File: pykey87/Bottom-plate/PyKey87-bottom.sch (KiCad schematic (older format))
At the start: 9 parts

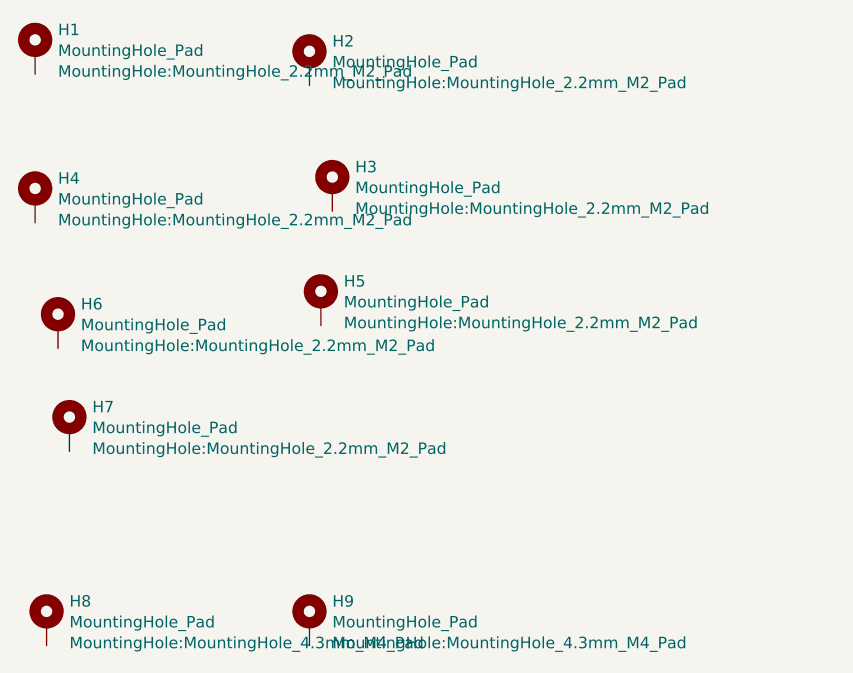
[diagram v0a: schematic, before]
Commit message: Moving things around
Prep for merging. Also did some clean up and added 8th standoff.
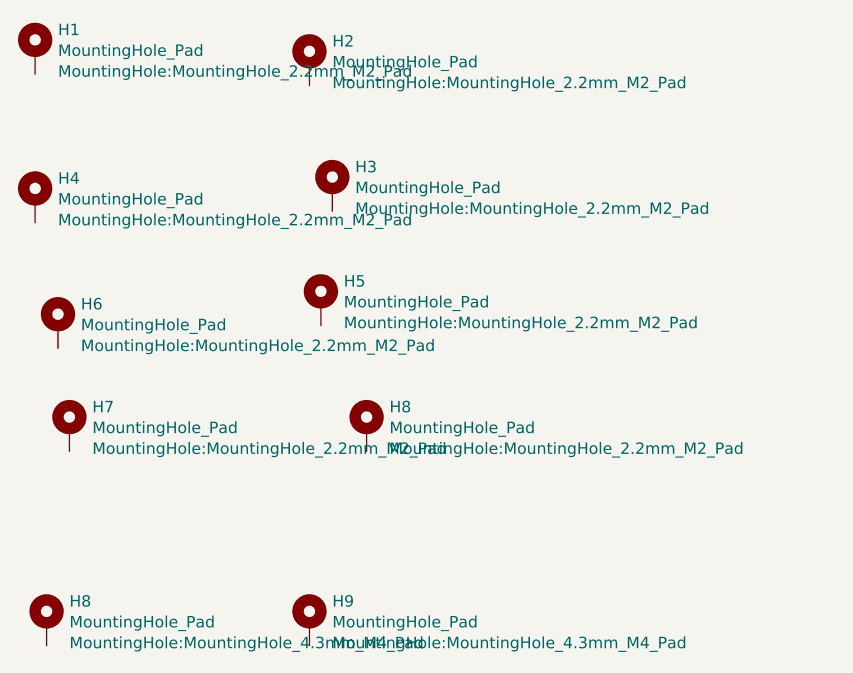
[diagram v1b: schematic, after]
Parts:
- added H8: MountingHole_Pad, MountingHole:MountingHole_2.2mm_M2_Pad, symbol Mechanical:MountingHole_Pad
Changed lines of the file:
@@
+	1    0    0    -1
+$EndComp
+$Comp
+L Mechanical:MountingHole_Pad H8
+U 1 1 618F6366
+P 3750 4150
+F 0 "H8" H 3850 4244 50  0000 L CNN
+F 1 "MountingHole_Pad" H 3850 4153 50  0000 L CNN
+F 2 "MountingHole:MountingHole_2.2mm_M2_Pad" H 3850 4062 50  0000 L CNN
+F 3 "~" H 3750 4150 50  0001 C CNN
+	1    3750 4150
 	1    0    0    -1
 $EndComp

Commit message: Working on issues
https://github.com/jpconstantineau/PyKey60/issues/3
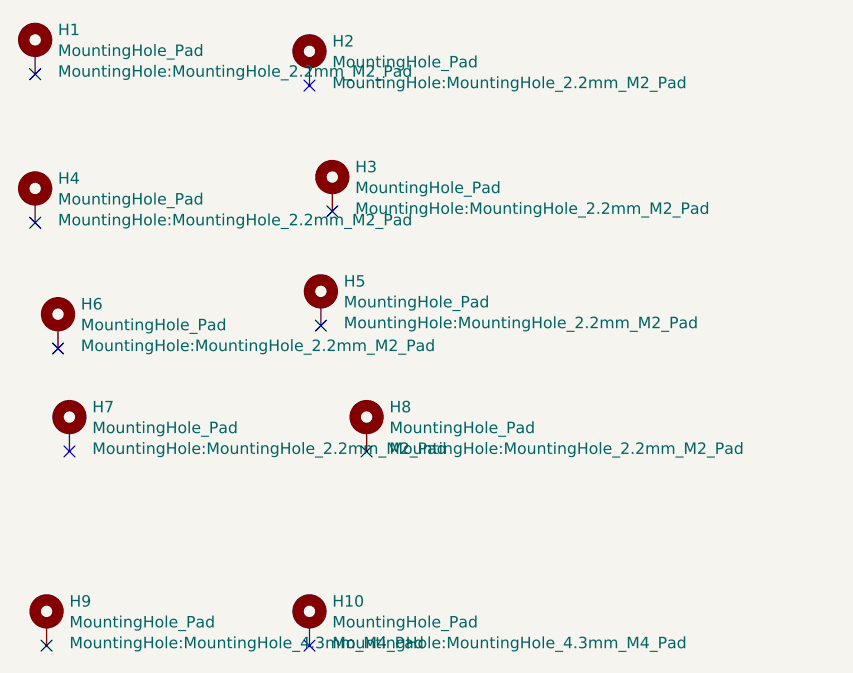
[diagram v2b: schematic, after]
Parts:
- renumbered H9 to H10, H8 to H9
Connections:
- no-connect marks 0 -> 10
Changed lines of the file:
@@
-$EndComp
-$Comp
-L Mechanical:MountingHole_Pad H1
-U 1 1 618E2AF4
-P 2300 2500
-F 0 "H1" H 2400 2594 50  0000 L CNN
-F 1 "MountingHole_Pad" H 2400 2503 50  0000 L CNN
-F 2 "MountingHole:MountingHole_2.2mm_M2_Pad" H 2400 2412 50  0000 L CNN
-F 3 "~" H 2300 2500 50  0001 C CNN
-	1    2300 2500
-	1    0    0    -1
 $EndComp
 $Comp
@@
 $EndComp
 $Comp
-L Mechanical:MountingHole_Pad H8
+L Mechanical:MountingHole_Pad H9
 U 1 1 618E47BC
 P 2350 5000
-F 0 "H8" H 2450 5094 50  0000 L CNN
+F 0 "H9" H 2450 5094 50  0000 L CNN
 F 1 "MountingHole_Pad" H 2450 5003 50  0000 L CNN
 F 2 "MountingHole:MountingHole_4.3mm_M4_Pad" H 2450 4912 50  0000 L CNN
@@
 $EndComp
 $Comp
-L Mechanical:MountingHole_Pad H9
+L Mechanical:MountingHole_Pad H10
 U 1 1 618E4FDD
 P 3500 5000
-F 0 "H9" H 3600 5094 50  0000 L CNN
+F 0 "H10" H 3600 5094 50  0000 L CNN
 F 1 "MountingHole_Pad" H 3600 5003 50  0000 L CNN
 F 2 "MountingHole:MountingHole_4.3mm_M4_Pad" H 3600 4912 50  0000 L CNN
@@
 	1    0    0    -1
 $EndComp
+$Comp
+L Mechanical:MountingHole_Pad H1
+U 1 1 618E2AF4
+P 2300 2500
+F 0 "H1" H 2400 2594 50  0000 L CNN
+F 1 "MountingHole_Pad" H 2400 2503 50  0000 L CNN
+F 2 "MountingHole:MountingHole_2.2mm_M2_Pad" H 2400 2412 50  0000 L CNN
+F 3 "~" H 2300 2500 50  0001 C CNN
+	1    2300 2500
+	1    0    0    -1
+$EndComp
+NoConn ~ 2300 2600
+NoConn ~ 2300 3250
+NoConn ~ 2400 3800
+NoConn ~ 2450 4250
+NoConn ~ 3500 2650
+NoConn ~ 3600 3200
+NoConn ~ 3550 3700
+NoConn ~ 3750 4250
+NoConn ~ 2350 5100
+NoConn ~ 3500 5100
 $EndSCHEMATC
